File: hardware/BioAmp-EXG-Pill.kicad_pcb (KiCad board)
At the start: 2 copper layers, 25.4 x 10 mm, 30 parts, among them J1 BioAmp Output, J2 BioAmp Input, U1 Amp, U2 LOGO_UDLABS

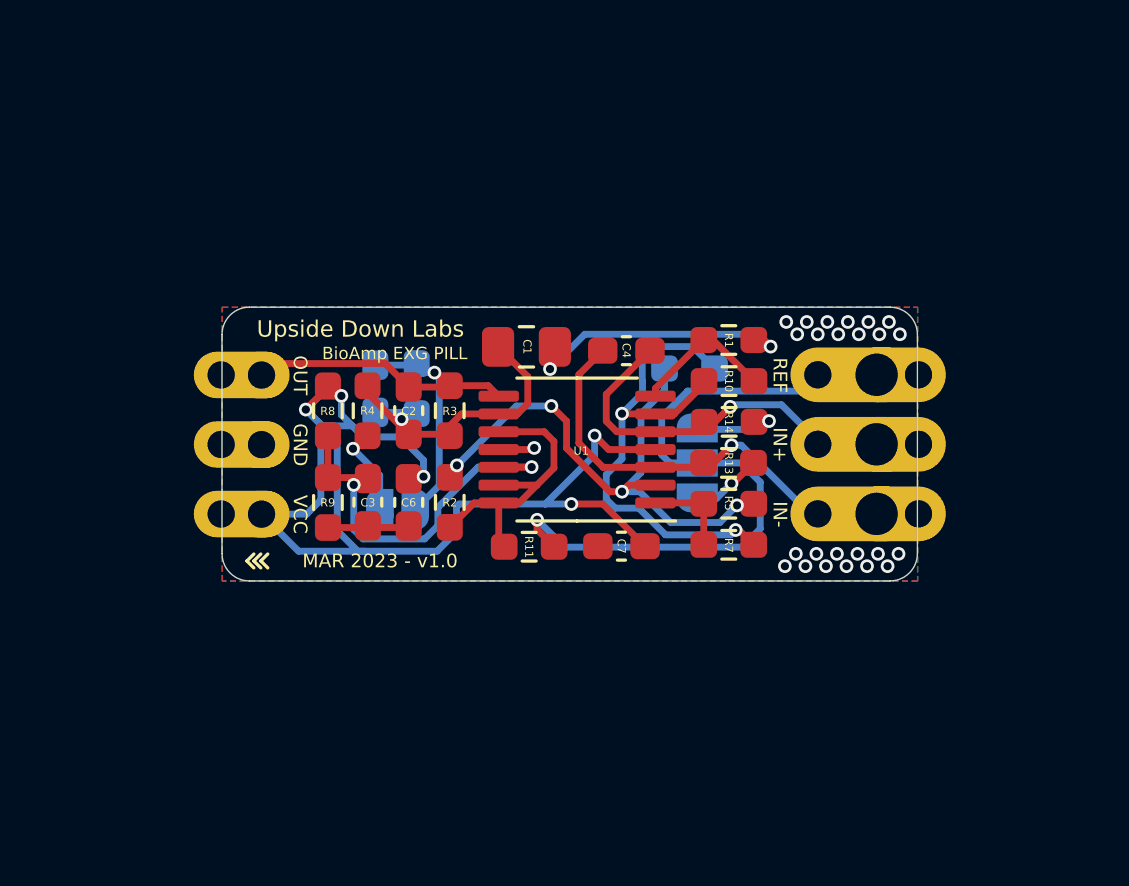
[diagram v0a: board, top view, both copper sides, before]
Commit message: add 2 power connectors for assembly in chain
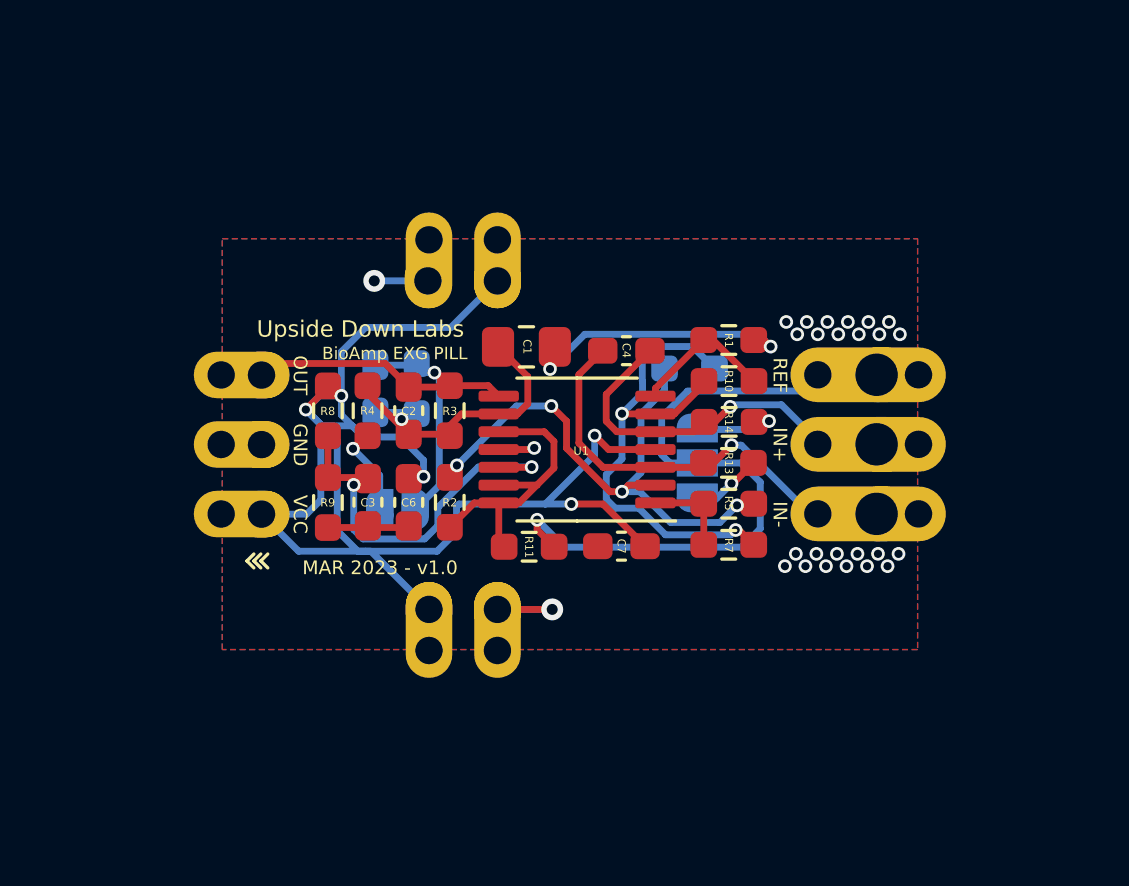
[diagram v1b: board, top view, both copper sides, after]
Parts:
- added ?: , , F.Cu at (118.5, 102.0)
- added ?: , , F.Cu at (121.0, 100.5)
- added ?: , , F.Cu at (121.0, 87.0)
- added ?: , , F.Cu at (121.0, 88.5)
- added ?: , , F.Cu at (118.5, 100.5)
- added ?: , , F.Cu at (118.5, 87.0)
- added ?: , , F.Cu at (118.5, 88.5)
- added ?: , , F.Cu at (121.0, 102.0)
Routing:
- net VCC: track 44.6 -> 56.2 mm
- net GND: track 4.30 -> 10.2 mm, vias 25 -> 27
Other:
- board outline removed

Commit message: add connectors and fill in ground
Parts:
- removed ? (x8): , 
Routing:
- net VCC: track 56.2 -> 44.6 mm
- net GND: track 10.2 -> 4.30 mm, vias 27 -> 25
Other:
- board outline added: 25.4 x 10 mm

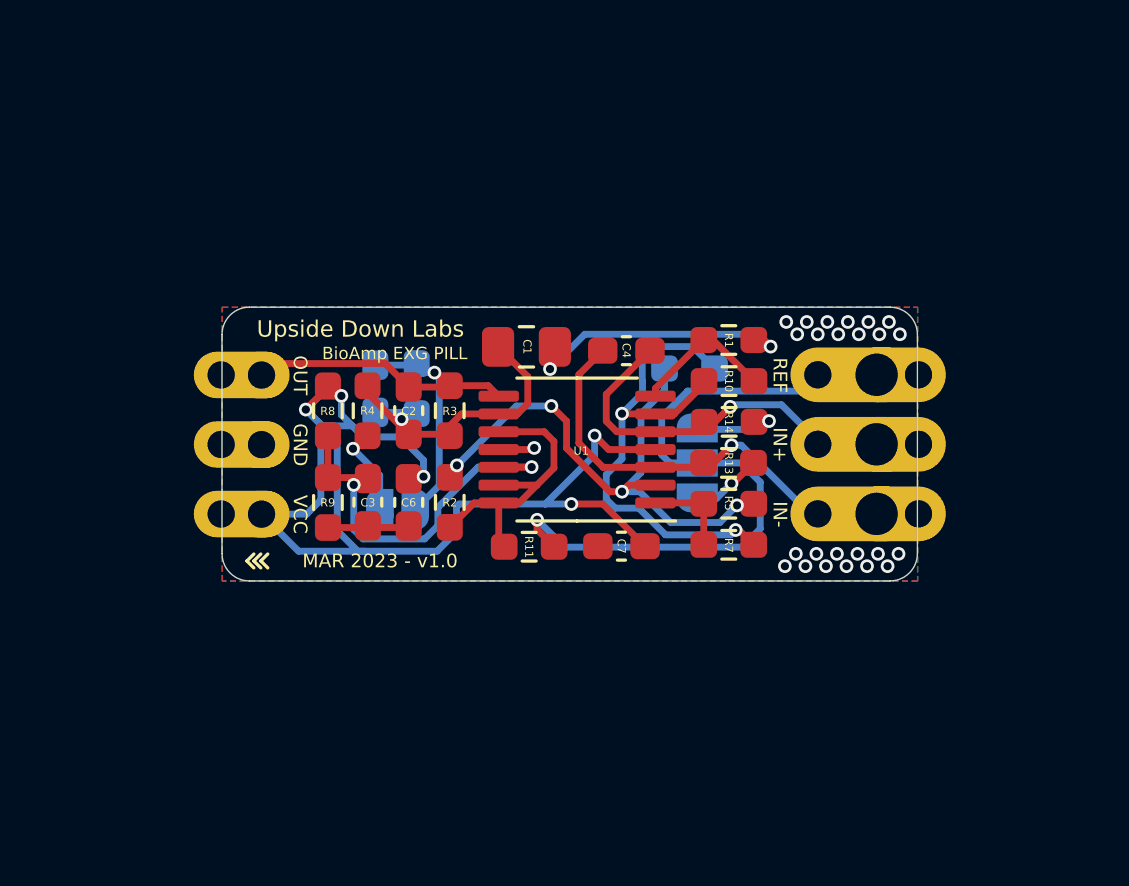
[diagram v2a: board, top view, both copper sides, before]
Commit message: shrink the pcb's dimensions
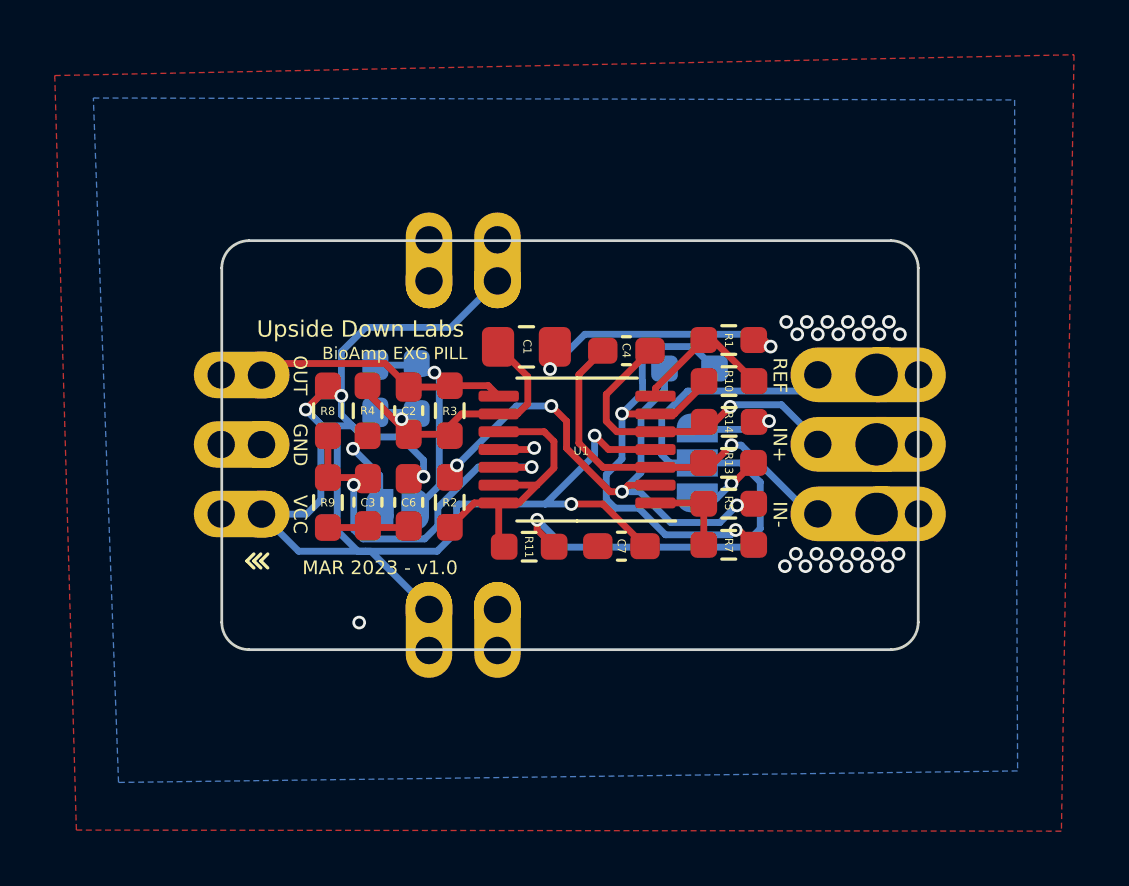
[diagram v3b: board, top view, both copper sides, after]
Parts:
- added ?: , , F.Cu at (118.5, 102.0)
- added ?: , , F.Cu at (121.0, 100.5)
- added ?: , , F.Cu at (121.0, 87.0)
- added ?: , , F.Cu at (121.0, 88.5)
- added ?: , , F.Cu at (118.5, 100.5)
- added ?: , , F.Cu at (118.5, 87.0)
- added ?: , , F.Cu at (118.5, 88.5)
- added ?: , , F.Cu at (121.0, 102.0)
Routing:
- net VCC: track 44.6 -> 56.2 mm
- net GND: vias 25 -> 26
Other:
- board size 25.4 x 10 mm -> 25.4 x 14.9 mm
